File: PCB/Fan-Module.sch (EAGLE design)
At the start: 26 parts, among them U1 ATSAMD11C14A-SSUT_ATSAMD11C14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, U3 LDL1117S12R_LDL1117S12R

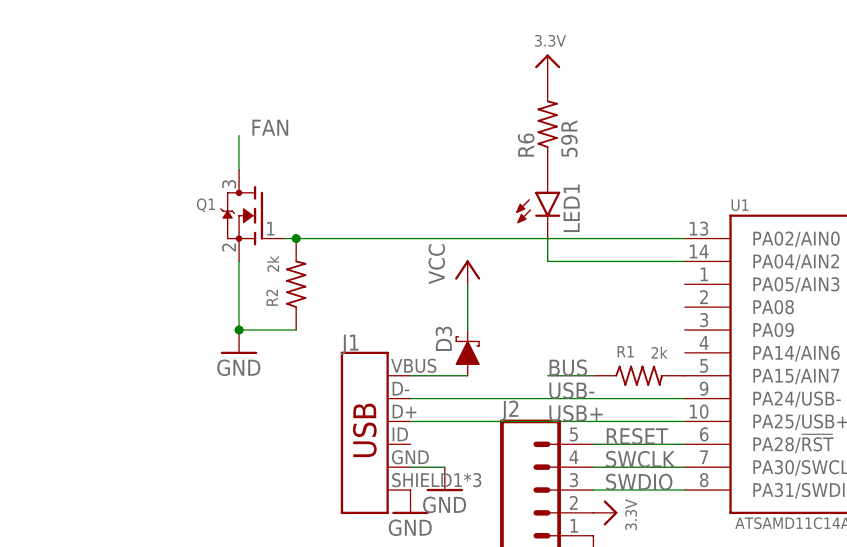
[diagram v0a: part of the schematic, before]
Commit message: added button to pcbs and did some fixing
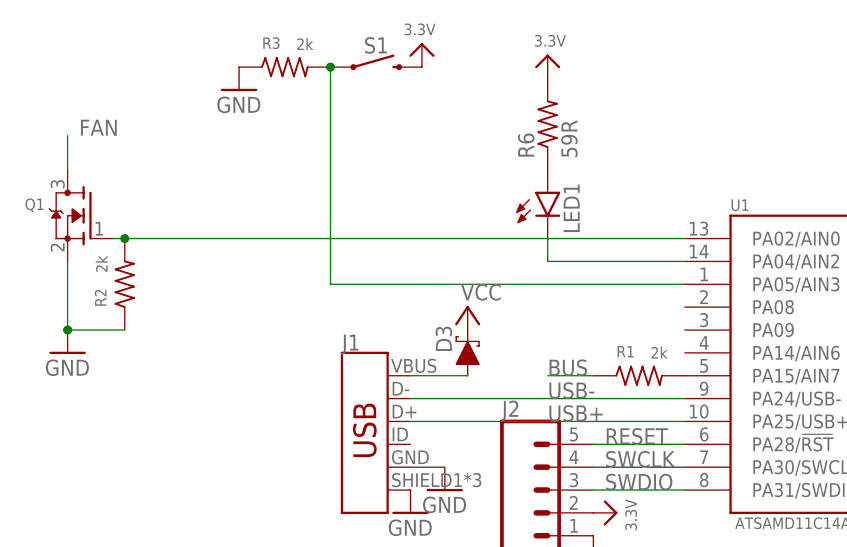
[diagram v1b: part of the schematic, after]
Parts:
- added R3: 2k, rcl:R-US_R1206
- added S1: MOMENTARY-SWITCH-SPST-SMD-6.0X3.5MM, SparkFun-Switches:MOMENTARY-SWITCH-SPST-SMD-6.0X3.5MM
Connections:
- new net N$7: R3.2, S1.1, U1.PA05/AIN3
- net 3.3V: now also S1.2
- net GND: now also R3.1
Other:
- moved on the sheet: Q1, R2
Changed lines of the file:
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@@
 <?xml version="1.0" encoding="utf-8"?>
 <!DOCTYPE eagle SYSTEM "eagle.dtd">
-<eagle version="9.3.0">
+<eagle version="9.2.2">
 <drawing>
 <settings>
@@
 <part name="R2" library="rcl" library_urn="urn:adsk.eagle:library:334" deviceset="R-US_" device="R1206" package3d_urn="urn:adsk.eagle:package:23540/2" value="2k"/>
 <part name="U1" library="LED-Board" deviceset="ATSAMD11C14A-SSUT_ATSAMD11C14A-SSUT" device=""/>
+<part name="U$6" library="microbuilder" deviceset="3.3V" device=""/>
+<part name="GND14" library="SparkFun-Aesthetics" deviceset="GND" device=""/>
+<part name="R3" library="rcl" library_urn="urn:adsk.eagle:library:334" deviceset="R-US_" device="R1206" package3d_urn="urn:adsk.eagle:package:23540/2" value="2k"/>
+<part name="S1" library="SparkFun-Switches" deviceset="MOMENTARY-SWITCH-SPST" device="-SMD-6.0X3.5MM"/>
 </parts>
 <sheets>
@@
 <attribute name="NAME" x="-61.4426" y="40.64" size="1.778" layer="95" rot="R90"/>
 </instance>
-<instance part="P+1" gate="VCC" x="-59.69" y="50.8" smashed="yes">
-<attribute name="VALUE" x="-62.23" y="48.26" size="1.778" layer="96" rot="R90"/>
+<instance part="P+1" gate="VCC" x="-59.69" y="45.72" smashed="yes">
+<attribute name="VALUE" x="-55.88" y="48.26" size="1.778" layer="96" rot="R180"/>
 </instance>
 <instance part="F1" gate="G$1" x="-1.27" y="0" smashed="yes">
@@
 <attribute name="VALUE" x="43.18" y="57.15" size="1.778" layer="96" rot="R270"/>
 </instance>
-<instance part="Q1" gate="G$1" x="-82.55" y="55.88" smashed="yes" rot="MR0">
-<attribute name="NAME" x="-87.63" y="56.515" size="1.27" layer="95" rot="MR0"/>
-<attribute name="VALUE" x="-87.63" y="54.61" size="1.27" layer="96" rot="MR0"/>
-</instance>
-<instance part="GND13" gate="1" x="-85.09" y="40.64" smashed="yes">
-<attribute name="VALUE" x="-87.63" y="38.1" size="1.778" layer="96"/>
-</instance>
-<instance part="R2" gate="G$1" x="-78.74" y="48.26" smashed="yes" rot="R90">
-<attribute name="NAME" x="-80.772" y="45.72" size="1.27" layer="95" font="vector" rot="R90"/>
-<attribute name="VALUE" x="-80.645" y="49.53" size="1.27" layer="96" font="vector" rot="R90"/>
+<instance part="Q1" gate="G$1" x="-101.6" y="55.88" smashed="yes" rot="MR0">
+<attribute name="NAME" x="-106.68" y="56.515" size="1.27" layer="95" rot="MR0"/>
+<attribute name="VALUE" x="-106.68" y="54.61" size="1.27" layer="96" rot="MR0"/>
+</instance>
+<instance part="GND13" gate="1" x="-104.14" y="40.64" smashed="yes">
+<attribute name="VALUE" x="-106.68" y="38.1" size="1.778" layer="96"/>
+</instance>
+<instance part="R2" gate="G$1" x="-97.79" y="48.26" smashed="yes" rot="R90">
+<attribute name="NAME" x="-99.822" y="45.72" size="1.27" layer="95" font="vector" rot="R90"/>
+<attribute name="VALUE" x="-99.695" y="49.53" size="1.27" layer="96" font="vector" rot="R90"/>
 </instance>
 <instance part="U1" gate="G$1" x="-20.32" y="40.64" smashed="yes">
 <attribute name="NAME" x="-30.5025" y="56.4229" size="1.272809375" layer="95"/>
 <attribute name="VALUE" x="-29.97303125" y="21.0799" size="1.27013125" layer="96"/>
+</instance>
+<instance part="U$6" gate="G$1" x="-64.77" y="74.93" smashed="yes" rot="MR0">
+<attribute name="VALUE" x="-63.246" y="75.946" size="1.27" layer="96" rot="MR0"/>
+</instance>
+<instance part="GND14" gate="1" x="-85.09" y="69.85" smashed="yes">
+<attribute name="VALUE" x="-87.63" y="67.31" size="1.778" layer="96"/>
+</instance>
+<instance part="R3" gate="G$1" x="-80.01" y="72.39" smashed="yes">
+<attribute name="NAME" x="-82.55" y="74.422" size="1.27" layer="95" font="vector"/>
+<attribute name="VALUE" x="-78.74" y="74.295" size="1.27" layer="96" font="vector"/>
+</instance>
+<instance part="S1" gate="G$1" x="-69.85" y="72.39" smashed="yes">
+<attribute name="NAME" x="-69.85" y="73.914" size="1.778" layer="95" font="vector" align="bottom-center"/>
 </instance>
 </instances>
@@
 <pinref part="R2" gate="G$1" pin="1"/>
 <pinref part="GND13" gate="1" pin="GND"/>
-<wire x1="-78.74" y1="43.18" x2="-85.09" y2="43.18" width="0.1524" layer="91"/>
+<wire x1="-97.79" y1="43.18" x2="-104.14" y2="43.18" width="0.1524" layer="91"/>
 <pinref part="Q1" gate="G$1" pin="S"/>
-<wire x1="-85.09" y1="50.8" x2="-85.09" y2="43.18" width="0.1524" layer="91"/>
-<junction x="-85.09" y="43.18"/>
+<wire x1="-104.14" y1="50.8" x2="-104.14" y2="43.18" width="0.1524" layer="91"/>
+<junction x="-104.14" y="43.18"/>
 </segment>
 <segment>
 <pinref part="U1" gate="G$1" pin="GND"/>
 <pinref part="GND2" gate="1" pin="GND"/>
+</segment>
+<segment>
+<pinref part="R3" gate="G$1" pin="1"/>
+<pinref part="GND14" gate="1" pin="GND"/>
 </segment>
 </net>
@@
 <wire x1="76.2" y1="3.81" x2="76.2" y2="1.27" width="0.1524" layer="91"/>
 </segment>
+<segment>
+<pinref part="S1" gate="G$1" pin="2"/>
+<pinref part="U$6" gate="G$1" pin="3.3V"/>
+</segment>
 </net>
 <net name="N$1" class="0">
@@
 <pinref part="D3" gate="G$1" pin="C"/>
 <pinref part="P+1" gate="VCC" pin="VCC"/>
-<wire x1="-59.69" y1="43.18" x2="-59.69" y2="48.26" width="0.1524" layer="91"/>
 </segment>
 <segment>
@@
 <segment>
 <pinref part="Q1" gate="G$1" pin="D"/>
-<wire x1="-85.09" y1="60.96" x2="-85.09" y2="64.77" width="0.1524" layer="91"/>
-<label x="-83.82" y="64.77" size="1.778" layer="95"/>
+<wire x1="-104.14" y1="60.96" x2="-104.14" y2="64.77" width="0.1524" layer="91"/>
+<label x="-102.87" y="64.77" size="1.778" layer="95"/>
 </segment>
 </net>
 <net name="N$5" class="0">
 <segment>
-<wire x1="-35.56" y1="53.34" x2="-78.74" y2="53.34" width="0.1524" layer="91"/>
+<wire x1="-35.56" y1="53.34" x2="-97.79" y2="53.34" width="0.1524" layer="91"/>
 <pinref part="Q1" gate="G$1" pin="G"/>
 <pinref part="R2" gate="G$1" pin="2"/>
-<wire x1="-78.74" y1="53.34" x2="-80.01" y2="53.34" width="0.1524" layer="91"/>
-<junction x="-78.74" y="53.34"/>
+<wire x1="-97.79" y1="53.34" x2="-99.06" y2="53.34" width="0.1524" layer="91"/>
+<junction x="-97.79" y="53.34"/>
 <pinref part="U1" gate="G$1" pin="PA02/AIN0"/>
 </segment>
@@
 </segment>
 </net>
+<net name="N$7" class="0">
+<segment>
+<pinref part="R3" gate="G$1" pin="2"/>
+<pinref part="S1" gate="G$1" pin="1"/>
+<pinref part="U1" gate="G$1" pin="PA05/AIN3"/>
+<wire x1="-35.56" y1="48.26" x2="-74.93" y2="48.26" width="0.1524" layer="91"/>
+<wire x1="-74.93" y1="48.26" x2="-74.93" y2="72.39" width="0.1524" layer="91"/>
+<junction x="-74.93" y="72.39"/>
+</segment>
+</net>

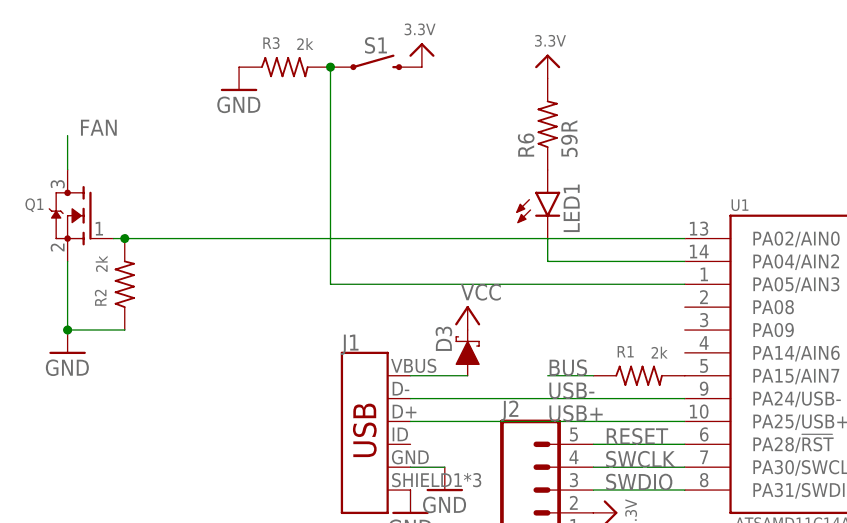
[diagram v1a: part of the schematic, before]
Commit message: added missing resistor before mosfet
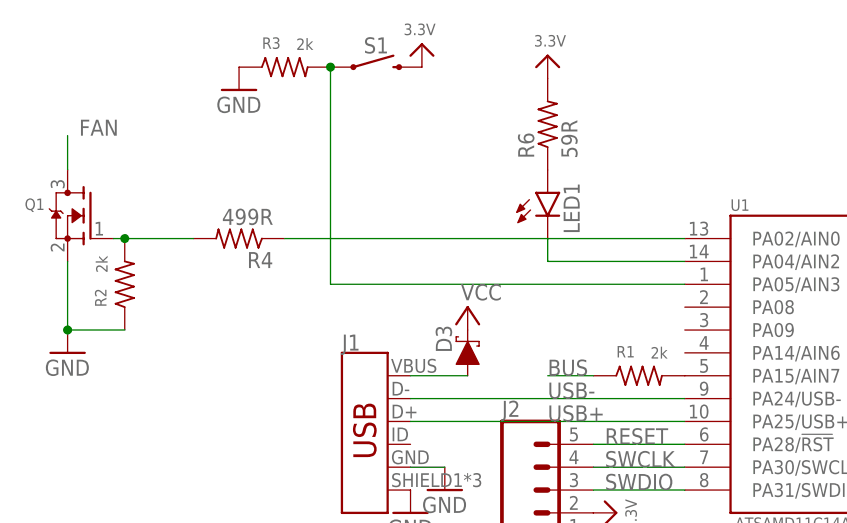
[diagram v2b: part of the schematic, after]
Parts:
- added R4: 499R, rcl:R-US_R0805
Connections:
- new net N$8: Q1.G, R2.2, R4.2
- net N$5: now also R4.1; no longer Q1.G, R2.2
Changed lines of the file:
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@@
 <?xml version="1.0" encoding="utf-8"?>
 <!DOCTYPE eagle SYSTEM "eagle.dtd">
-<eagle version="9.2.2">
+<eagle version="9.3.0">
 <drawing>
 <settings>
@@
 <part name="R3" library="rcl" library_urn="urn:adsk.eagle:library:334" deviceset="R-US_" device="R1206" package3d_urn="urn:adsk.eagle:package:23540/2" value="2k"/>
 <part name="S1" library="SparkFun-Switches" deviceset="MOMENTARY-SWITCH-SPST" device="-SMD-6.0X3.5MM"/>
+<part name="R4" library="rcl" library_urn="urn:adsk.eagle:library:334" deviceset="R-US_" device="R0805" package3d_urn="urn:adsk.eagle:package:23553/2" value="499R"/>
 </parts>
 <sheets>
@@
 <attribute name="NAME" x="-69.85" y="73.914" size="1.778" layer="95" font="vector" align="bottom-center"/>
 </instance>
+<instance part="R4" gate="G$1" x="-85.09" y="53.34" smashed="yes" rot="R180">
+<attribute name="NAME" x="-81.28" y="51.8414" size="1.778" layer="95" rot="R180"/>
+<attribute name="VALUE" x="-81.28" y="56.642" size="1.778" layer="96" rot="R180"/>
+</instance>
 </instances>
 <busses>
@@
 <net name="N$5" class="0">
 <segment>
-<wire x1="-35.56" y1="53.34" x2="-97.79" y2="53.34" width="0.1524" layer="91"/>
-<pinref part="Q1" gate="G$1" pin="G"/>
-<pinref part="R2" gate="G$1" pin="2"/>
-<wire x1="-97.79" y1="53.34" x2="-99.06" y2="53.34" width="0.1524" layer="91"/>
-<junction x="-97.79" y="53.34"/>
+<wire x1="-35.56" y1="53.34" x2="-80.01" y2="53.34" width="0.1524" layer="91"/>
 <pinref part="U1" gate="G$1" pin="PA02/AIN0"/>
+<pinref part="R4" gate="G$1" pin="1"/>
 </segment>
 </net>
@@
 </segment>
 </net>
+<net name="N$8" class="0">
+<segment>
+<pinref part="Q1" gate="G$1" pin="G"/>
+<pinref part="R2" gate="G$1" pin="2"/>
+<wire x1="-97.79" y1="53.34" x2="-99.06" y2="53.34" width="0.1524" layer="91"/>
+<junction x="-97.79" y="53.34"/>
+<wire x1="-90.17" y1="53.34" x2="-97.79" y2="53.34" width="0.1524" layer="91"/>
+<pinref part="R4" gate="G$1" pin="2"/>
+</segment>
+</net>

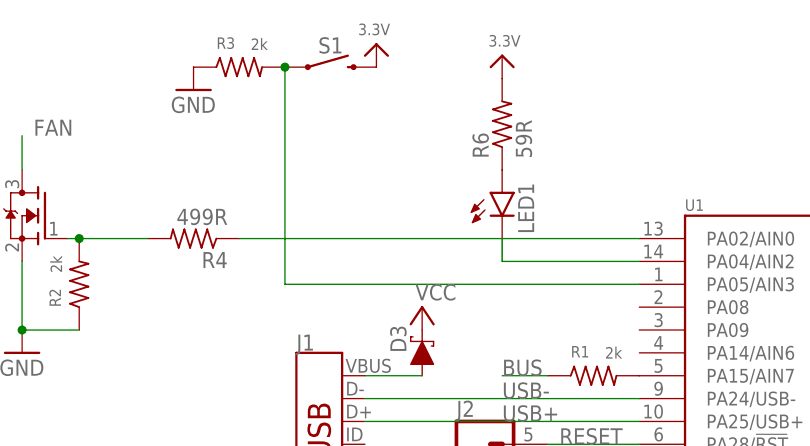
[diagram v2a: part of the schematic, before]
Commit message: removed buttons.. not needed
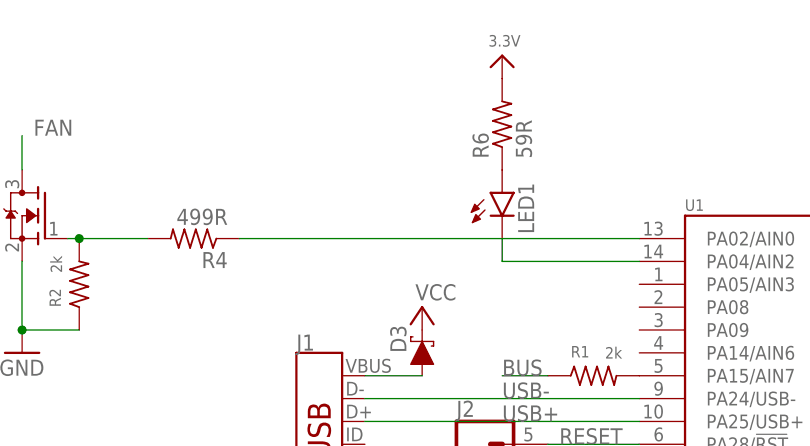
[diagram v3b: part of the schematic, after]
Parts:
- removed R3: 2k, rcl:R-US_R1206
- removed S1: MOMENTARY-SWITCH-SPST-SMD-6.0X3.5MM, SparkFun-Switches:MOMENTARY-SWITCH-SPST-SMD-6.0X3.5MM
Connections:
- removed net N$7: R3.2, S1.1, U1.PA05/AIN3
- net 3.3V: no longer S1.2
- net GND: no longer R3.1
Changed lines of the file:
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@@
 <part name="R2" library="rcl" library_urn="urn:adsk.eagle:library:334" deviceset="R-US_" device="R1206" package3d_urn="urn:adsk.eagle:package:23540/2" value="2k"/>
 <part name="U1" library="LED-Board" deviceset="ATSAMD11C14A-SSUT_ATSAMD11C14A-SSUT" device=""/>
-<part name="U$6" library="microbuilder" deviceset="3.3V" device=""/>
-<part name="GND14" library="SparkFun-Aesthetics" deviceset="GND" device=""/>
-<part name="R3" library="rcl" library_urn="urn:adsk.eagle:library:334" deviceset="R-US_" device="R1206" package3d_urn="urn:adsk.eagle:package:23540/2" value="2k"/>
-<part name="S1" library="SparkFun-Switches" deviceset="MOMENTARY-SWITCH-SPST" device="-SMD-6.0X3.5MM"/>
 <part name="R4" library="rcl" library_urn="urn:adsk.eagle:library:334" deviceset="R-US_" device="R0805" package3d_urn="urn:adsk.eagle:package:23553/2" value="499R"/>
 </parts>
@@
 <attribute name="VALUE" x="-29.97303125" y="21.0799" size="1.27013125" layer="96"/>
 </instance>
-<instance part="U$6" gate="G$1" x="-64.77" y="74.93" smashed="yes" rot="MR0">
-<attribute name="VALUE" x="-63.246" y="75.946" size="1.27" layer="96" rot="MR0"/>
-</instance>
-<instance part="GND14" gate="1" x="-85.09" y="69.85" smashed="yes">
-<attribute name="VALUE" x="-87.63" y="67.31" size="1.778" layer="96"/>
-</instance>
-<instance part="R3" gate="G$1" x="-80.01" y="72.39" smashed="yes">
-<attribute name="NAME" x="-82.55" y="74.422" size="1.27" layer="95" font="vector"/>
-<attribute name="VALUE" x="-78.74" y="74.295" size="1.27" layer="96" font="vector"/>
-</instance>
-<instance part="S1" gate="G$1" x="-69.85" y="72.39" smashed="yes">
-<attribute name="NAME" x="-69.85" y="73.914" size="1.778" layer="95" font="vector" align="bottom-center"/>
-</instance>
 <instance part="R4" gate="G$1" x="-85.09" y="53.34" smashed="yes" rot="R180">
 <attribute name="NAME" x="-81.28" y="51.8414" size="1.778" layer="95" rot="R180"/>
@@
 <pinref part="GND2" gate="1" pin="GND"/>
 </segment>
-<segment>
-<pinref part="R3" gate="G$1" pin="1"/>
-<pinref part="GND14" gate="1" pin="GND"/>
-</segment>
 </net>
 <net name="VCC-RAW" class="1">
@@
 <wire x1="76.2" y1="3.81" x2="76.2" y2="1.27" width="0.1524" layer="91"/>
 </segment>
-<segment>
-<pinref part="S1" gate="G$1" pin="2"/>
-<pinref part="U$6" gate="G$1" pin="3.3V"/>
-</segment>
 </net>
 <net name="N$1" class="0">
@@
 </segment>
 </net>
-<net name="N$7" class="0">
-<segment>
-<pinref part="R3" gate="G$1" pin="2"/>
-<pinref part="S1" gate="G$1" pin="1"/>
-<pinref part="U1" gate="G$1" pin="PA05/AIN3"/>
-<wire x1="-35.56" y1="48.26" x2="-74.93" y2="48.26" width="0.1524" layer="91"/>
-<wire x1="-74.93" y1="48.26" x2="-74.93" y2="72.39" width="0.1524" layer="91"/>
-<junction x="-74.93" y="72.39"/>
-</segment>
-</net>
